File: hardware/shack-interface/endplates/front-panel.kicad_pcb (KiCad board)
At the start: 2 copper layers, 165 x 51.1 mm, 4 parts

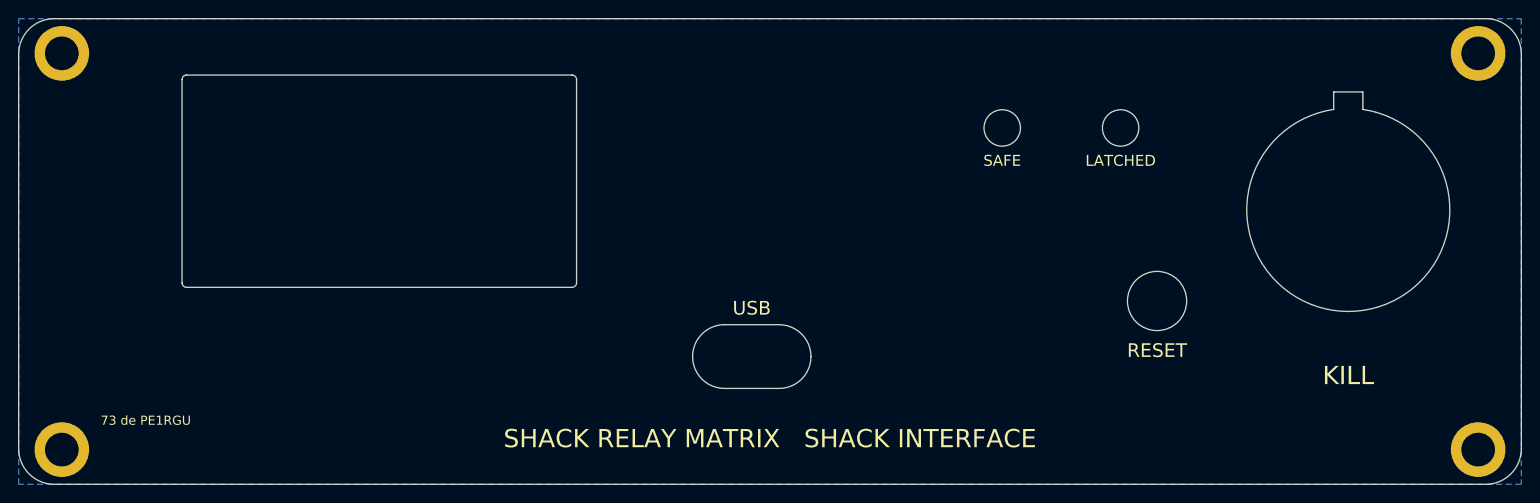
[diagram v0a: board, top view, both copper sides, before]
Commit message: Shack interface: 2 inch display, front plate a8, board p8b, full render
- D-186, M-102: layout p7, J14 (USB-C) at the rear edge; rear plate a7.
- D-187, M-103: Waveshare 2inch LCD (240x320 IPS, ST7789VW); front plate a8;
  new printed display frame on WA-SMSI 9774055151R spacers.
- M-104, M-105: layout p8b with the display notch, routed 155 of 155, DRC 0.
- M-106: full SolidCraft render (case/render-full/); README open-case view.

Co-Authored-By: Claude Opus 5.5 <noreply@anthropic.com>
Claude-Session: https://claude.ai/code/session_01B1V8swdbsr8c87yrmmzj34
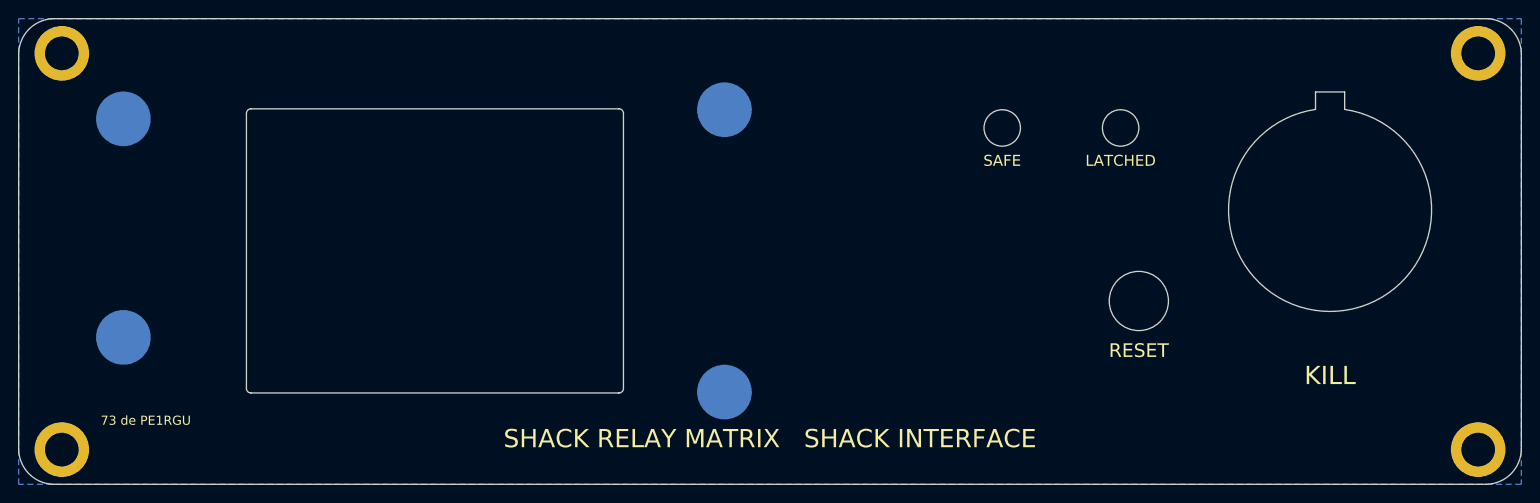
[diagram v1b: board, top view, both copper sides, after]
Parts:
- added SP1: , , B.Cu at (31.5, 31.0)
- added SP2: , , B.Cu at (31.5, 55.0)
- added SP3: , , B.Cu at (97.5, 30.0)
- added SP4: , , B.Cu at (97.5, 61.0)
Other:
- outline, holes or cut-outs redrawn
- board text added: "SP1 to SP4: WA-SMSI 9774055151R"
- board text added: "SRM shack interface front plate rev A (a8) 2026-10"
- board text removed: "SRM shack interface front plate rev A (a3) 2026-10"
- board text removed: "USB"
